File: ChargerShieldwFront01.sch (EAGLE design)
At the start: 93 parts, among them IC1 TL431, IC2 LM324N, Q1 BUZ11, Q2 BD648, Q3 BUZ171, Q4 BUZ11, Q5 BD648, Q6 BUZ171, T1 BC548, T2 BC548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

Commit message: upd
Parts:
- R25: device rcl:R-EU_0207/12 -> rcl:R-EU_0207/10
- R27: device rcl:R-EU_0207/10 -> rcl:R-EU_0207/12
- R28: device rcl:R-EU_0207/10 -> rcl:R-EU_0207/15
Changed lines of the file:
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@@
 <grid distance="0.05" unitdist="inch" unit="mm" style="lines" multiple="1" display="yes" altdistance="0.025" altunitdist="inch" altunit="mm"/>
 <layers>
-<layer number="1" name="Top" color="4" fill="1" visible="no" active="no"/>
-<layer number="2" name="Route2" color="1" fill="3" visible="no" active="no"/>
-<layer number="3" name="Route3" color="4" fill="3" visible="no" active="no"/>
-<layer number="4" name="Route4" color="1" fill="4" visible="no" active="no"/>
-<layer number="5" name="Route5" color="4" fill="4" visible="no" active="no"/>
-<layer number="6" name="Route6" color="1" fill="8" visible="no" active="no"/>
-<layer number="7" name="Route7" color="4" fill="8" visible="no" active="no"/>
-<layer number="8" name="Route8" color="1" fill="2" visible="no" active="no"/>
-<layer number="9" name="Route9" color="4" fill="2" visible="no" active="no"/>
-<layer number="10" name="Route10" color="1" fill="7" visible="no" active="no"/>
-<layer number="11" name="Route11" color="4" fill="7" visible="no" active="no"/>
-<layer number="12" name="Route12" color="1" fill="5" visible="no" active="no"/>
-<layer number="13" name="Route13" color="4" fill="5" visible="no" active="no"/>
-<layer number="14" name="Route14" color="1" fill="6" visible="no" active="no"/>
-<layer number="15" name="Route15" color="4" fill="6" visible="no" active="no"/>
-<layer number="16" name="Bottom" color="1" fill="1" visible="no" active="no"/>
-<layer number="17" name="Pads" color="2" fill="1" visible="no" active="no"/>
-<layer number="18" name="Vias" color="2" fill="1" visible="no" active="no"/>
-<layer number="19" name="Unrouted" color="6" fill="1" visible="no" active="no"/>
-<layer number="20" name="Dimension" color="15" fill="1" visible="no" active="no"/>
-<layer number="21" name="tPlace" color="7" fill="1" visible="no" active="no"/>
-<layer number="22" name="bPlace" color="7" fill="1" visible="no" active="no"/>
-<layer number="23" name="tOrigins" color="15" fill="1" visible="no" active="no"/>
-<layer number="24" name="bOrigins" color="15" fill="1" visible="no" active="no"/>
-<layer number="25" name="tNames" color="7" fill="1" visible="no" active="no"/>
-<layer number="26" name="bNames" color="7" fill="1" visible="no" active="no"/>
-<layer number="27" name="tValues" color="7" fill="1" visible="no" active="no"/>
-<layer number="28" name="bValues" color="7" fill="1" visible="no" active="no"/>
+<layer number="1" name="Top" color="4" fill="1" visible="yes" active="no"/>
+<layer number="2" name="Route2" color="1" fill="3" visible="yes" active="no"/>
+<layer number="3" name="Route3" color="4" fill="3" visible="yes" active="no"/>
+<layer number="4" name="Route4" color="1" fill="4" visible="yes" active="no"/>
+<layer number="5" name="Route5" color="4" fill="4" visible="yes" active="no"/>
+<layer number="6" name="Route6" color="1" fill="8" visible="yes" active="no"/>
+<layer number="7" name="Route7" color="4" fill="8" visible="yes" active="no"/>
+<layer number="8" name="Route8" color="1" fill="2" visible="yes" active="no"/>
+<layer number="9" name="Route9" color="4" fill="2" visible="yes" active="no"/>
+<layer number="10" name="Route10" color="1" fill="7" visible="yes" active="no"/>
+<layer number="11" name="Route11" color="4" fill="7" visible="yes" active="no"/>
+<layer number="12" name="Route12" color="1" fill="5" visible="yes" active="no"/>
+<layer number="13" name="Route13" color="4" fill="5" visible="yes" active="no"/>
+<layer number="14" name="Route14" color="1" fill="6" visible="yes" active="no"/>
+<layer number="15" name="Route15" color="4" fill="6" visible="yes" active="no"/>
+<layer number="16" name="Bottom" color="1" fill="1" visible="yes" active="no"/>
+<layer number="17" name="Pads" color="2" fill="1" visible="yes" active="no"/>
+<layer number="18" name="Vias" color="2" fill="1" visible="yes" active="no"/>
+<layer number="19" name="Unrouted" color="6" fill="1" visible="yes" active="no"/>
+<layer number="20" name="Dimension" color="15" fill="1" visible="yes" active="no"/>
+<layer number="21" name="tPlace" color="7" fill="1" visible="yes" active="no"/>
+<layer number="22" name="bPlace" color="7" fill="1" visible="yes" active="no"/>
+<layer number="23" name="tOrigins" color="15" fill="1" visible="yes" active="no"/>
+<layer number="24" name="bOrigins" color="15" fill="1" visible="yes" active="no"/>
+<layer number="25" name="tNames" color="7" fill="1" visible="yes" active="no"/>
+<layer number="26" name="bNames" color="7" fill="1" visible="yes" active="no"/>
+<layer number="27" name="tValues" color="7" fill="1" visible="yes" active="no"/>
+<layer number="28" name="bValues" color="7" fill="1" visible="yes" active="no"/>
 <layer number="29" name="tStop" color="7" fill="3" visible="no" active="no"/>
 <layer number="30" name="bStop" color="7" fill="6" visible="no" active="no"/>
@@
 <layer number="35" name="tGlue" color="7" fill="4" visible="no" active="no"/>
 <layer number="36" name="bGlue" color="7" fill="5" visible="no" active="no"/>
-<layer number="37" name="tTest" color="7" fill="1" visible="no" active="no"/>
-<layer number="38" name="bTest" color="7" fill="1" visible="no" active="no"/>
+<layer number="37" name="tTest" color="7" fill="1" visible="yes" active="no"/>
+<layer number="38" name="bTest" color="7" fill="1" visible="yes" active="no"/>
 <layer number="39" name="tKeepout" color="4" fill="11" visible="no" active="no"/>
 <layer number="40" name="bKeepout" color="1" fill="11" visible="no" active="no"/>
@@
 <layer number="44" name="Drills" color="7" fill="1" visible="no" active="no"/>
 <layer number="45" name="Holes" color="7" fill="1" visible="no" active="no"/>
-<layer number="46" name="Milling" color="3" fill="1" visible="no" active="no"/>
-<layer number="47" name="Measures" color="7" fill="1" visible="no" active="no"/>
-<layer number="48" name="Document" color="7" fill="1" visible="no" active="no"/>
-<layer number="49" name="Reference" color="7" fill="1" visible="no" active="no"/>
-<layer number="50" name="dxf" color="7" fill="1" visible="no" active="no"/>
-<layer number="51" name="tDocu" color="7" fill="1" visible="no" active="no"/>
-<layer number="52" name="bDocu" color="7" fill="1" visible="no" active="no"/>
-<layer number="53" name="tGND_GNDA" color="7" fill="9" visible="no" active="no"/>
-<layer number="54" name="bGND_GNDA" color="1" fill="9" visible="no" active="no"/>
-<layer number="56" name="wert" color="7" fill="1" visible="no" active="no"/>
-<layer number="57" name="tCAD" color="7" fill="1" visible="no" active="no"/>
+<layer number="46" name="Milling" color="3" fill="1" visible="yes" active="no"/>
+<layer number="47" name="Measures" color="7" fill="1" visible="yes" active="no"/>
+<layer number="48" name="Document" color="7" fill="1" visible="yes" active="no"/>
+<layer number="49" name="Reference" color="7" fill="1" visible="yes" active="no"/>
+<layer number="50" name="dxf" color="7" fill="1" visible="yes" active="no"/>
+<layer number="51" name="tDocu" color="7" fill="1" visible="yes" active="no"/>
+<layer number="52" name="bDocu" color="7" fill="1" visible="yes" active="no"/>
+<layer number="53" name="tGND_GNDA" color="7" fill="9" visible="yes" active="no"/>
+<layer number="54" name="bGND_GNDA" color="1" fill="9" visible="yes" active="no"/>
+<layer number="56" name="wert" color="7" fill="1" visible="yes" active="no"/>
+<layer number="57" name="tCAD" color="7" fill="1" visible="yes" active="no"/>
 <layer number="91" name="Nets" color="2" fill="1" visible="yes" active="yes"/>
 <layer number="92" name="Busses" color="1" fill="1" visible="yes" active="yes"/>
@@
 <part name="X4" library="con-wago-500" deviceset="W237-4" device="" value="Battery"/>
 <part name="T2" library="transistor" deviceset="BC238" device="" value="BC548"/>
-<part name="R28" library="rcl" deviceset="R-EU_" device="0207/10" value="2k2"/>
+<part name="R28" library="rcl" deviceset="R-EU_" device="0207/15" value="2k2"/>
 <part name="R32" library="rcl" deviceset="R-EU_" device="0207/10" value="1k"/>
 <part name="C7" library="rcl" deviceset="C-EU" device="025_050-025X075" value="15n/60V"/>
@@
 <part name="R30" library="rcl" deviceset="R-EU_" device="0207/10" value="12k"/>
 <part name="GND22" library="supply1" deviceset="GND" device=""/>
-<part name="R25" library="rcl" deviceset="R-EU_" device="0207/12" value="1k"/>
+<part name="R25" library="rcl" deviceset="R-EU_" device="0207/10" value="1k"/>
 <part name="Q4" library="transistor-fet" deviceset="BUZ11" device=""/>
 <part name="P+10" library="supply1" deviceset="+5V" device=""/>
-<part name="R27" library="rcl" deviceset="R-EU_" device="0207/10" value="1k"/>
+<part name="R27" library="rcl" deviceset="R-EU_" device="0207/12" value="1k"/>
 <part name="C6" library="rcl" deviceset="CPOL-EU" device="E5-5" value="3µ3"/>
 <part name="Q6" library="transistor-fet" deviceset="BUZ171" device=""/>

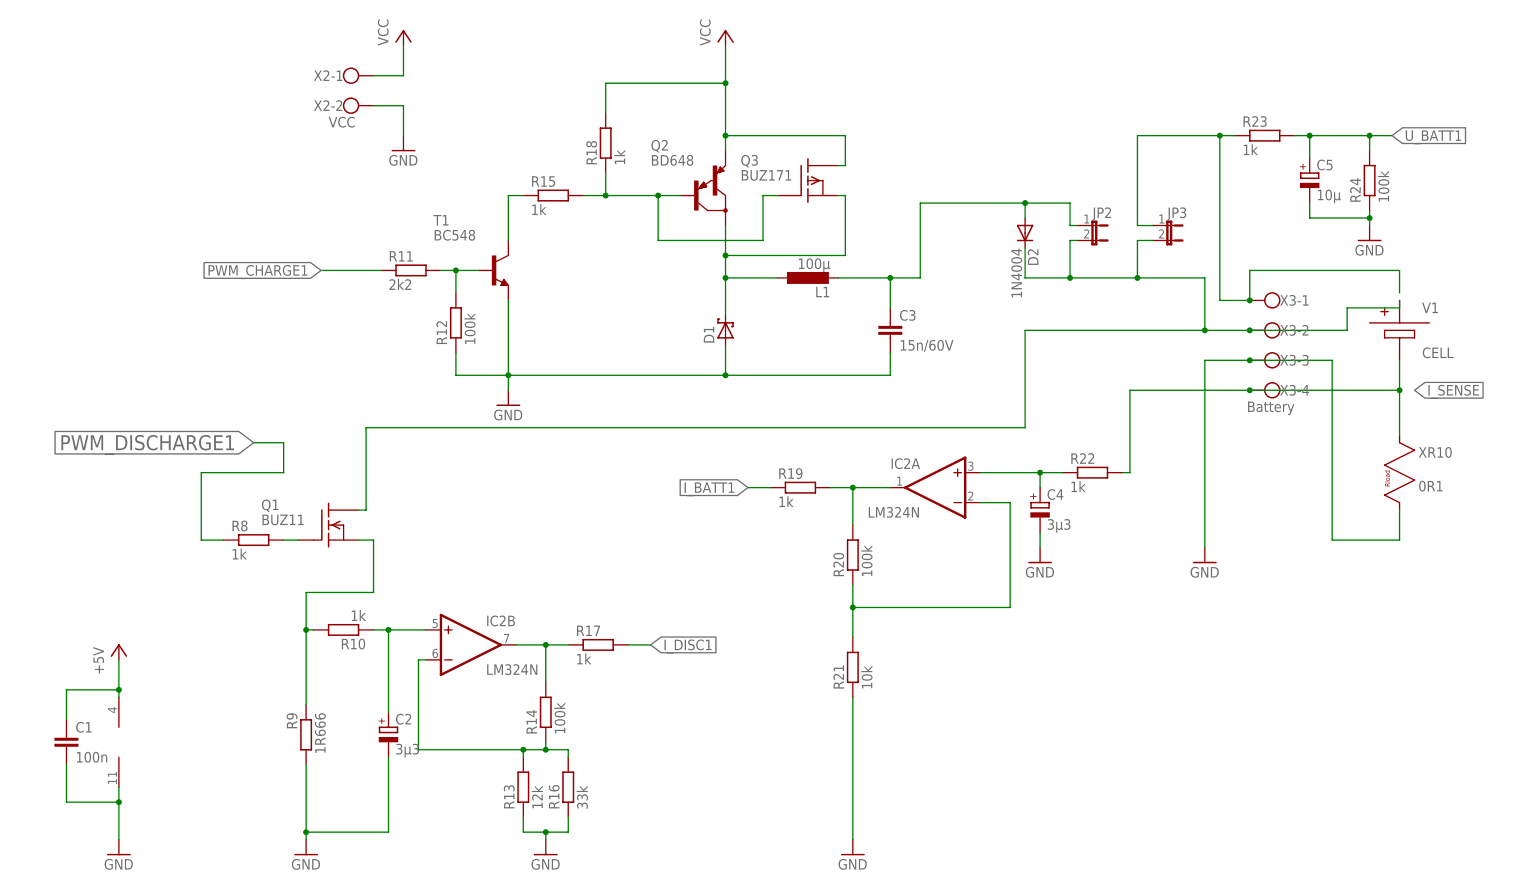
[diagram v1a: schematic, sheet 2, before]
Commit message: difference amplifier at charge current
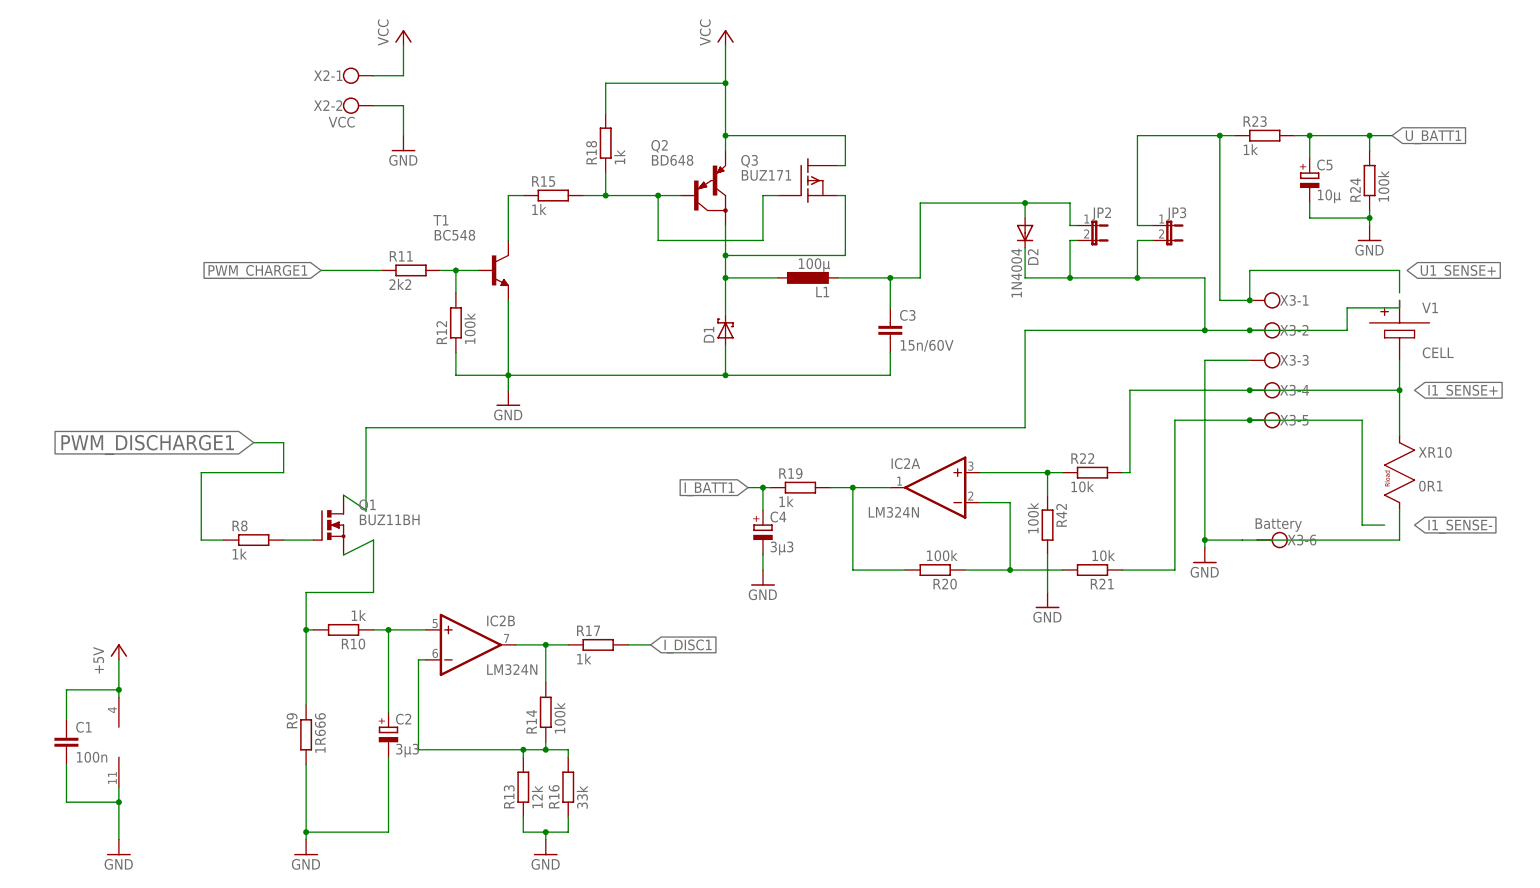
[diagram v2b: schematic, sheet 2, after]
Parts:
- added R42: 100k, rcl:R-EU_0204/7
- Q1, Q4: value BUZ11 -> BUZ11BH; device transistor-fet:BUZ11 -> transistor-power:BUZ11BH
- R21: device rcl:R-EU_0204/7 -> rcl:R-EU_0207/12
- R22: value 1k -> 10k
- X3, X4: device con-wago-500:W237-4 -> con-wago-500:W237-6
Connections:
- net I_SENSE renamed I1_SENSE+
- net N$8 renamed U1_SENSE+
- new net I1_SENSE-: R21.1, X3-5.KL
- net GND: now also R42.2, X3-6.KL, X4-6.KL; no longer R21.1, X4-3.KL
- net I_BATT1: now also C4.+
- net N$15: now also R42.1; no longer C4.+
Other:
- moved on the sheet: C4, R20, R21
